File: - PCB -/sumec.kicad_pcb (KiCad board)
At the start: 2 copper layers, 95 x 73 mm, 30 parts, among them IC1 XT30U-F, SW1 SW_SPDT, SW3 SW_Push, U1 ESP32-DEVKIT-V1, U10 LD1117AV33, U11 ROB-14450, U2 VL53L0X, U3 VL53L0X, U4 VL53L0X, U5 TSOP382xx, U6 QRE1113, U7 QRE1113, U8 QRE1113, U9 QRE1113

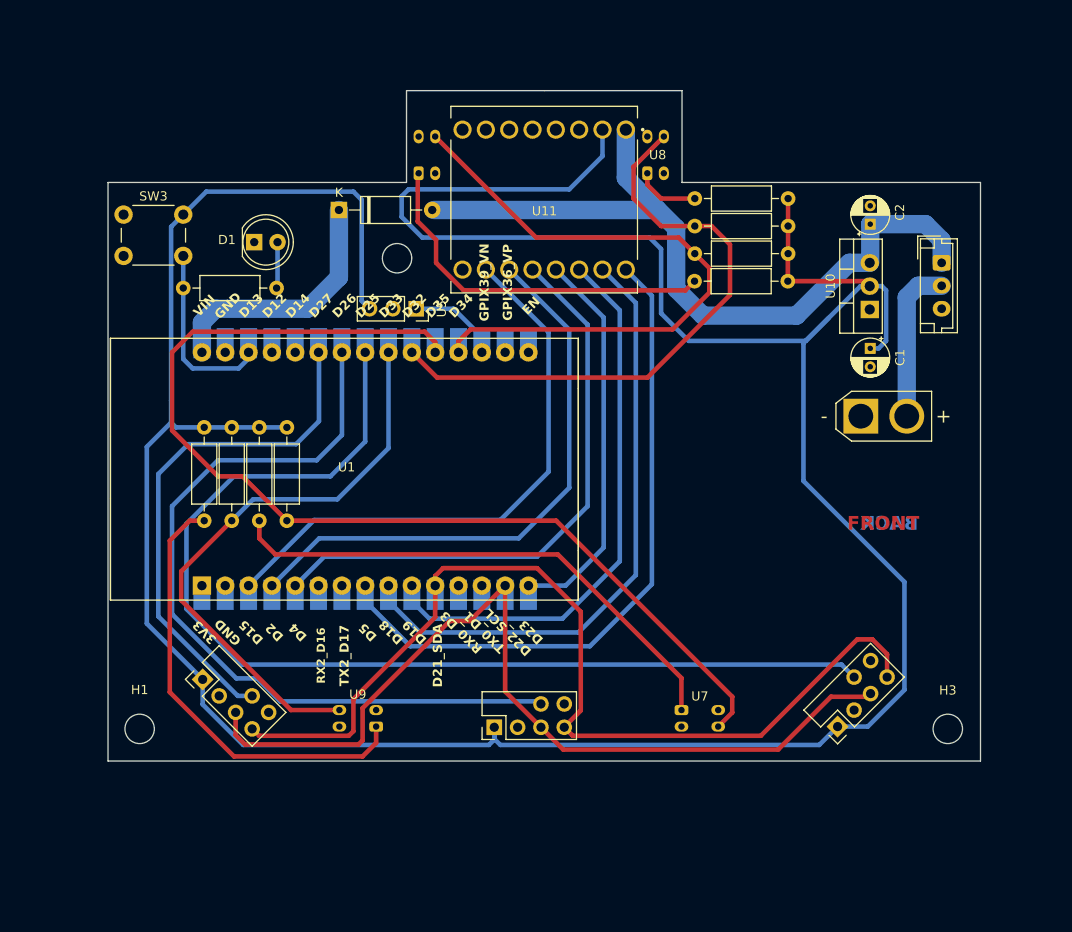
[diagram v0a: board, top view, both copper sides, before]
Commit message: PCB almost wired
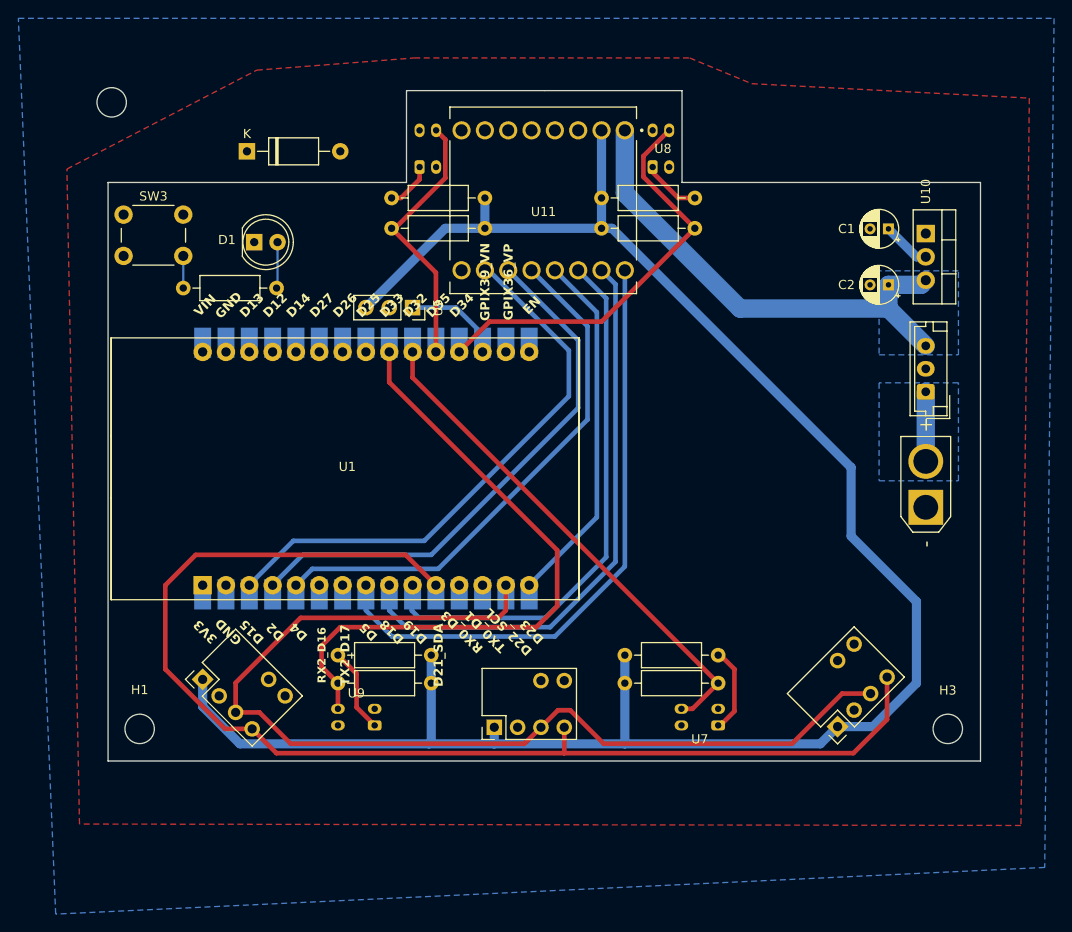
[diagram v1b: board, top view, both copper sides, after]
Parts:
- moved R4 52.1 mm to (156.5, 109.5), turned to 180 degrees
- moved R5 46.2 mm to (146.3, 112.5), turned to 0 degrees
- moved H2 35.4 mm to (90.4, 49.3)
- moved R9 35.3 mm to (125.2, 112.5), turned to 180 degrees
- moved R2 34.2 mm to (120.9, 59.7)
- moved R3 33.1 mm to (131.1, 63.0)
- moved R8 20.7 mm to (115.1, 109.5), turned to 0 degrees
- moved R7 20.3 mm to (143.8, 63.0), turned to 0 degrees
- moved SW1 14.1 mm to (179.1, 80.8), turned to 90 degrees
- moved C1 13.2 mm to (175.0, 63.1), turned to 180 degrees
- moved IC1 12.2 mm to (179.1, 93.4), turned to 90 degrees
- moved D2 11.9 mm to (105.2, 54.6)
- moved U10 10.3 mm to (179.1, 63.6), turned to -90 degrees
- moved C2 6.90 mm to (175.0, 69.1), turned to 180 degrees
- moved U7 4.33 mm to (156.5, 117.1), turned to 90 degrees
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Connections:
- SW1 pad 1: +12V -> 12V IN
- SW1 pad 2: 12V IN -> unconnected-(SW1A-B-Pad2)
- SW1 pad 3: unconnected-(SW1A-C-Pad3) -> +12V
- U1 pad 19: QRE1113 A -> QRE1113 C
- U1 pad 20: QRE1113 B -> QRE1113 A
- U1 pad 21: QRE1113 C -> QRE1113 B
- U1 pad 23: X-SHUT 2 -> X-SHUT 1
- U1 pad 24: X-SHUT 3 -> X-SHUT 2
- U1 pad 25: X-SHUT 1 -> X-SHUT 3
- U2 pad 5: GPIO -> unconnected-(U2-GPIO-Pad5)
- U3 pad 5: GPIO -> unconnected-(U3-GPIO-Pad5)
- U4 pad 5: GPIO -> unconnected-(U4-GPIO-Pad5)
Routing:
- net +3V3: track 353.5 -> 219.2 mm
- net X-SHUT 2: track 117.9 -> 0.00 mm
- net X-SHUT 3: track 86.7 -> 0.00 mm
- net QRE1113 B: track 116.6 -> 55.0 mm
- net X-SHUT 1: track 56.7 -> 0.00 mm
- net Net-(U7-A): track 57.7 -> 9.40 mm
- net QRE1113 A: track 69.2 -> 29.2 mm
- net Net-(U9-A): track 48.9 -> 9.30 mm
- net Net-(U6-A): track 40.4 -> 5.22 mm
- net +12V: track 84.0 -> 53.4 mm
- net Net-(D2-K): track 27.5 -> 0.00 mm
- net SDA: track 106.7 -> 132.7 mm
- net QRE1113 C: track 65.7 -> 45.4 mm
- net SCL: track 97.9 -> 114.5 mm
- net TEST PROGRAM: track 19.9 -> 3.50 mm
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- added copper zone on B.Cu, net +12V
- added copper zone on B.Cu, net 12V IN
- added copper zone on B.Cu, net GND
- added copper zone on F.Cu, net GND
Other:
- board text removed: "BACK"
- board text removed: "FRONT"

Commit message: PCB - Board update
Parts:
- moved H2 74.0 mm to (163.2, 62.2)
- moved D2 31.4 mm to (136.1, 60.0)
- moved R3 19.8 mm to (113.2, 71.7), turned to 45 degrees
- moved R4 10.4 mm to (146.2, 107.5), turned to -90 degrees
- moved R5 6.00 mm to (149.5, 117.6), turned to 90 degrees
- moved R9 5.99 mm to (129.2, 117.0), turned to 135 degrees
- moved R8 3.97 mm to (118.8, 110.8), turned to -45 degrees
- moved R2 3.59 mm to (118.4, 62.3), turned to -135 degrees
- moved U11 1.41 mm to (137.4, 61.4)
- moved SW3 1.22 mm to (91.7, 62.7)
- moved R1 0.72 mm to (98.2, 70.2)
- moved D1 0.22 mm to (106.0, 64.7)
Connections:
- U1 pad 23: X-SHUT 1 -> X-SHUT 2
- U1 pad 24: X-SHUT 2 -> X-SHUT 3
- U1 pad 25: X-SHUT 3 -> X-SHUT 1
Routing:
- net X-SHUT 2: track 0.00 -> 110.4 mm
- net X-SHUT 3: track 0.00 -> 80.8 mm
- net Net-(D2-K): track 0.00 -> 58.9 mm
- net +3V3: track 219.2 -> 275.8 mm
- net X-SHUT 1: track 0.00 -> 53.4 mm
- net Net-(U7-A): track 9.40 -> 22.8 mm
- net TEST PROGRAM: track 3.50 -> 14.6 mm
- net QRE1113 D: track 70.3 -> 73.7 mm
- net Net-(U6-A): track 5.22 -> 8.40 mm
- net QRE1113 B: track 55.0 -> 57.8 mm
- net BI1: track 58.0 -> 55.6 mm
- net PWMB: track 61.1 -> 58.7 mm
- net BI2: track 59.4 -> 57.2 mm
- net STBY: track 39.2 -> 37.2 mm
- net AI1: track 59.4 -> 57.6 mm
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
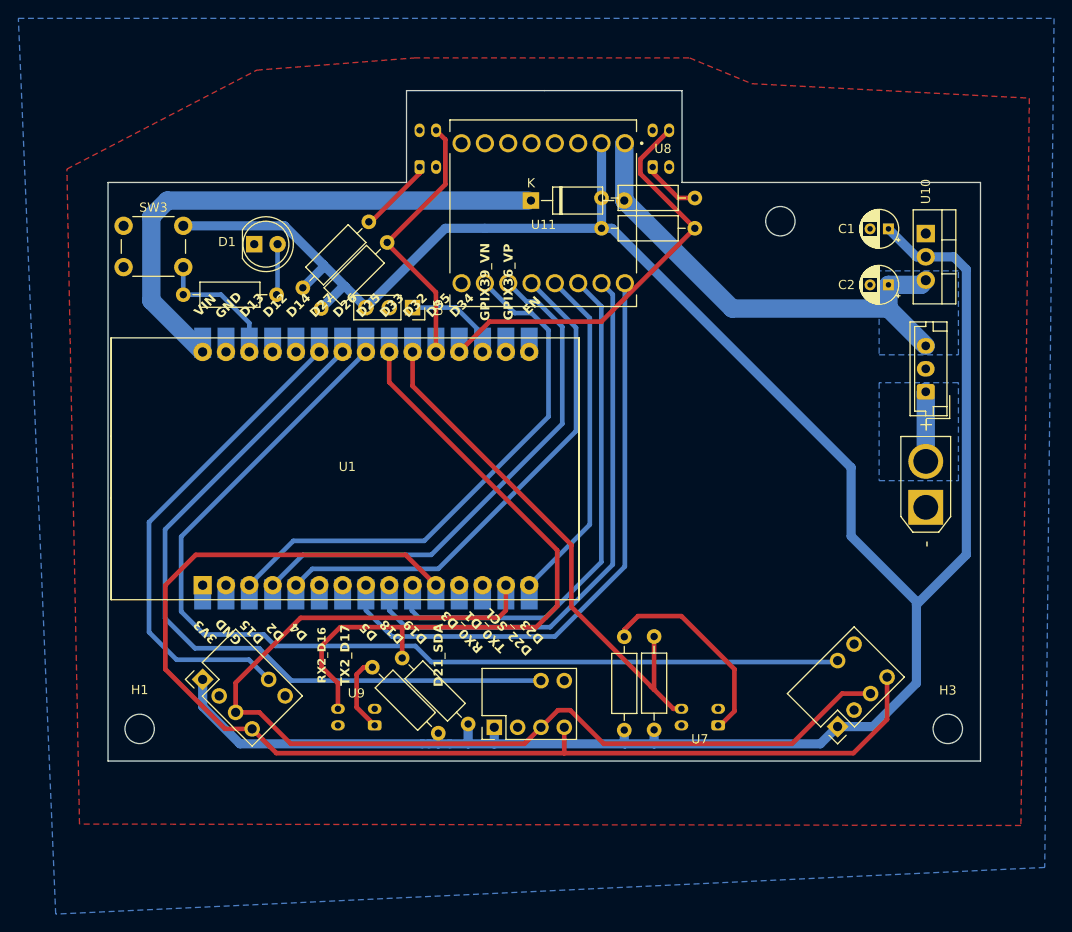
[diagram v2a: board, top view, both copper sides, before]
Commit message: PCB - Wiring control and fix
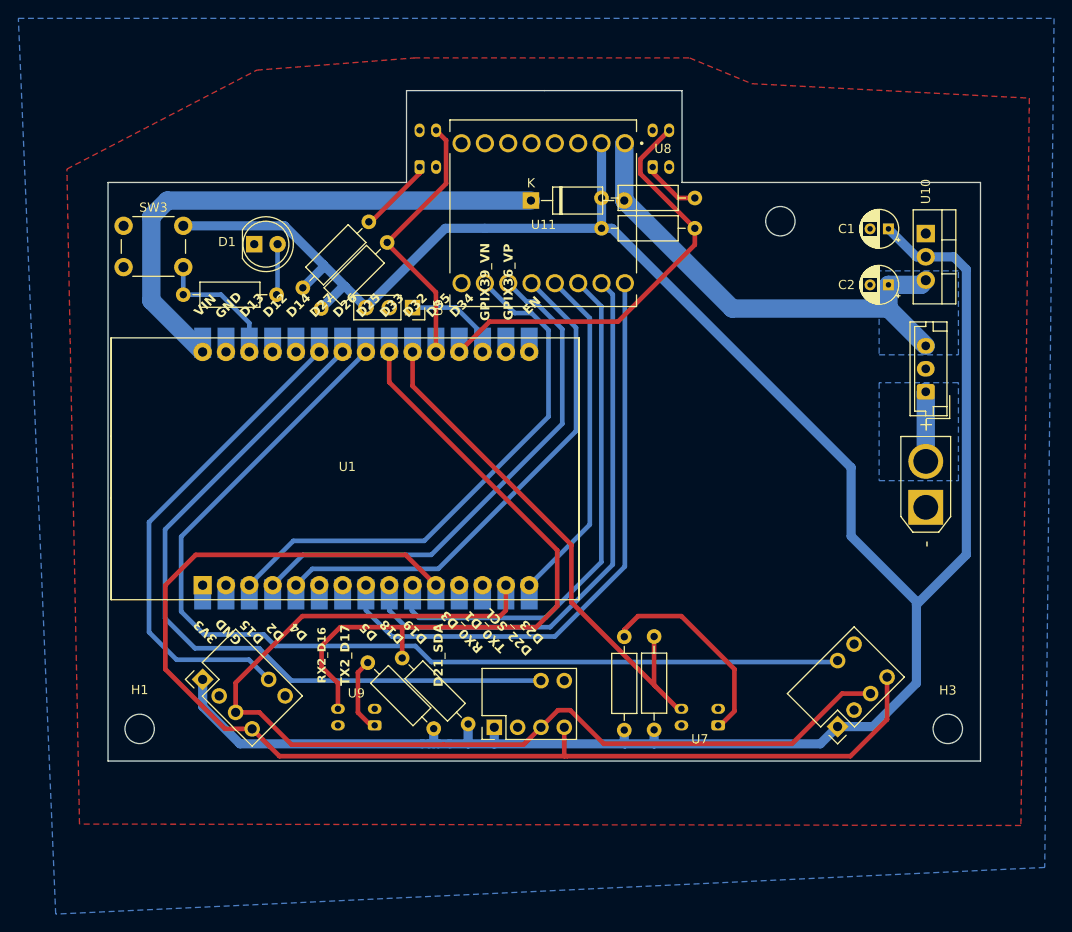
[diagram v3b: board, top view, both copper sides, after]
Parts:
- moved R8 0.71 mm to (118.3, 110.3)
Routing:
- net QRE1113 B: track 57.8 -> 56.7 mm
- net QRE1113 C: track 45.7 -> 46.7 mm
- net SDA: track 132.7 -> 133.3 mm

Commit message: PCB - LED Signal. board upd
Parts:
- R1: value 75 -> 75
- moved R1 7.00 mm to (102.3, 64.5), turned to -45 degrees
- moved D1 6.92 mm to (103.0, 71.0), turned to 135 degrees
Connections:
- R1 pad 1: TEST PROGRAM -> Net-(D1-A)
- R1 pad 2: Net-(D1-A) -> LED SIGNALISATION
- U1 pad 26: unconnected-(U1-D14-Pad26) -> LED SIGNALISATION
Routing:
- net LED SIGNALISATION: track 0.00 -> 5.15 mm
- net Net-(D1-A): track 4.83 -> 5.72 mm

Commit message: Update sumec.kicad_pcb
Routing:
- net QRE1113 D: track 73.7 -> 70.7 mm
- net QRE1113 B: track 56.7 -> 58.9 mm
- net QRE1113 C: track 46.7 -> 48.3 mm
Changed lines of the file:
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@@
   (segment (start 123.19 80.17) (end 140.49 97.47) (width 0.508) (layer "F.Cu") (net 9))
   (segment (start 152.086 115.316) (end 152.464 115.316) (width 0.508) (layer "F.Cu") (net 9))
-  (segment (start 149.615 112.845) (end 149.49 112.72) (width 0.508) (layer "F.Cu") (net 9))
   (segment (start 140.49 97.47) (end 140.49 103.72) (width 0.508) (layer "F.Cu") (net 9))
   (segment (start 123.19 76.454) (end 123.19 80.17) (width 0.508) (layer "F.Cu") (net 9))
   (segment (start 149.615 112.845) (end 152.086 115.316) (width 0.508) (layer "F.Cu") (net 9))
-  (segment (start 149.49 112.72) (end 149.49 107.442) (width 0.508) (layer "F.Cu") (net 9))
+  (segment (start 149.615 112.845) (end 146.851 110.081) (width 0.508) (layer "F.Cu") (net 9))
   (segment (start 140.49 103.72) (end 149.615 112.845) (width 0.508) (layer "F.Cu") (net 9))
+  (segment (start 146.851 110.081) (end 149.49 107.442) (width 0.508) (layer "F.Cu") (net 9))
   (segment (start 152.124 59.69) (end 153.924 59.69) (width 0.508) (layer "F.Cu") (net 10))
   (segment (start 149.33 56.896) (end 152.124 59.69) (width 0.508) (layer "F.Cu") (net 10))
+  (segment (start 151.13 52.324) (end 147.99 55.464) (width 0.508) (layer "F.Cu") (net 11))
+  (segment (start 128.8288 73.152) (end 145.558 73.152) (width 0.508) (layer "F.Cu") (net 11))
+  (segment (start 147.99 57.058) (end 153.924 62.992) (width 0.508) (layer "F.Cu") (net 11))
+  (segment (start 153.924 64.786) (end 153.924 62.992) (width 0.508) (layer "F.Cu") (net 11))
+  (segment (start 128.27 76.454) (end 128.27 73.7108) (width 0.508) (layer "F.Cu") (net 11))
+  (segment (start 128.27 73.7108) (end 128.8288 73.152) (width 0.508) (layer "F.Cu") (net 11))
   (segment (start 145.558 73.152) (end 153.924 64.786) (width 0.508) (layer "F.Cu") (net 11))
-  (segment (start 151.13 52.324) (end 147.99 55.464) (width 0.508) (layer "F.Cu") (net 11))
-  (segment (start 147.99 57.058) (end 153.924 62.992) (width 0.508) (layer "F.Cu") (net 11))
-  (segment (start 128.27 76.454) (end 131.572 73.152) (width 0.508) (layer "F.Cu") (net 11))
-  (segment (start 153.924 64.786) (end 153.924 62.992) (width 0.508) (layer "F.Cu") (net 11))
   (segment (start 147.99 55.464) (end 147.99 57.058) (width 0.508) (layer "F.Cu") (net 11))
-  (segment (start 131.572 73.152) (end 145.558 73.152) (width 0.508) (layer "F.Cu") (net 11))
   (segment (start 118.636 117.116) (end 119.062 117.116) (width 0.508) (layer "F.Cu") (net 12))
   (segment (start 117.24 111.35159) (end 117.24 115.72) (width 0.508) (layer "F.Cu") (net 12))
   (segment (start 118.305795 110.285795) (end 117.24 111.35159) (width 0.508) (layer "F.Cu") (net 12))
   (segment (start 117.24 115.72) (end 118.636 117.116) (width 0.508) (layer "F.Cu") (net 12))
+  (segment (start 118.0592 106.426) (end 115.062 109.4232) (width 0.508) (layer "F.Cu") (net 13))
   (segment (start 120.65 76.454) (end 120.65 79.756) (width 0.508) (layer "F.Cu") (net 13))
   (segment (start 136.652 106.426) (end 122.24 106.426) (width 0.508) (layer "F.Cu") (net 13))
-  (segment (start 113.284 110.744) (end 115.062 112.522) (width 0.508) (layer "F.Cu") (net 13))
   (segment (start 122.055795 106.610205) (end 122.055795 109.785795) (width 0.508) (layer "F.Cu") (net 13))
   (segment (start 138.938 98.044) (end 138.938 104.14) (width 0.508) (layer "F.Cu") (net 13))
   (segment (start 122.24 106.426) (end 122.055795 106.610205) (width 0.508) (layer "F.Cu") (net 13))
-  (segment (start 113.284 108.458) (end 113.284 110.744) (width 0.508) (layer "F.Cu") (net 13))
-  (segment (start 122.24 106.426) (end 115.316 106.426) (width 0.508) (layer "F.Cu") (net 13))
-  (segment (start 115.316 106.426) (end 113.284 108.458) (width 0.508) (layer "F.Cu") (net 13))
-  (segment (start 115.062 112.522) (end 115.062 115.316) (width 0.508) (layer "F.Cu") (net 13))
+  (segment (start 122.24 106.426) (end 118.0592 106.426) (width 0.508) (layer "F.Cu") (net 13))
+  (segment (start 115.062 109.4232) (end 115.062 115.316) (width 0.508) (layer "F.Cu") (net 13))
   (segment (start 120.65 79.756) (end 138.938 98.044) (width 0.508) (layer "F.Cu") (net 13))
   (segment (start 138.938 104.14) (end 136.652 106.426) (width 0.508) (layer "F.Cu") (net 13))
@@
   (segment (start 142.49 95.254) (end 135.89 101.854) (width 0.508) (layer "B.Cu") (net 24))
   (segment (start 138.684 68.97) (end 142.49 72.776) (width 0.508) (layer "B.Cu") (net 24))
+  (segment (start 140.99 85.07) (end 125.984 100.076) (width 0.508) (layer "B.Cu") (net 25))
   (segment (start 140.99 73.816) (end 140.99 85.07) (width 0.508) (layer "B.Cu") (net 25))
-  (segment (start 140.99 85.07) (end 125.984 100.076) (width 0.508) (layer "B.Cu") (net 25))
   (segment (start 125.984 100.076) (end 112.268 100.076) (width 0.508) (layer "B.Cu") (net 25))
   (segment (start 136.144 68.97) (end 140.99 73.816) (width 0.508) (layer "B.Cu") (net 25))
@@
   (segment (start 131.064 68.97) (end 134.314 72.22) (width 0.508) (layer "B.Cu") (net 27))
   (segment (start 136.134 72.22) (end 137.99 74.076) (width 0.508) (layer "B.Cu") (net 27))
-  (segment (start 147.74 105.22) (end 152.464 105.22) (width 0.508) (layer "F.Cu") (net 28))
-  (segment (start 146.24 106.72) (end 147.74 105.22) (width 0.508) (layer "F.Cu") (net 28))
+  (segment (start 146.24 107.47) (end 148.49 105.22) (width 0.508) (layer "F.Cu") (net 28))
+  (segment (start 148.49 105.22) (end 152.464 105.22) (width 0.508) (layer "F.Cu") (net 28))
+  (segment (start 152.464 105.22) (end 158.242 110.998) (width 0.508) (layer "F.Cu") (net 28))
+  (segment (start 158.242 110.998) (end 158.242 115.57) (width 0.508) (layer "F.Cu") (net 28))
+  (segment (start 156.696 117.116) (end 156.464 117.116) (width 0.508) (layer "F.Cu") (net 28))
   (segment (start 158.242 115.57) (end 156.696 117.116) (width 0.508) (layer "F.Cu") (net 28))
-  (segment (start 146.24 107.47) (end 146.24 106.72) (width 0.508) (layer "F.Cu") (net 28))
-  (segment (start 156.696 117.116) (end 156.464 117.116) (width 0.508) (layer "F.Cu") (net 28))
-  (segment (start 158.242 110.998) (end 158.242 115.57) (width 0.508) (layer "F.Cu") (net 28))
-  (segment (start 152.464 105.22) (end 158.242 110.998) (width 0.508) (layer "F.Cu") (net 28))
   (segment (start 94.49 106.97) (end 94.49 94.994) (width 0.508) (layer "B.Cu") (net 32))
   (segment (start 105.374204 109.97) (end 97.49 109.97) (width 0.508) (layer "B.Cu") (net 32))
@@
   (segment (start 107.516051 112.111847) (end 105.374204 109.97) (width 0.508) (layer "B.Cu") (net 32))
   (segment (start 169.47 110.065795) (end 169.315795 110.22) (width 0.25) (layer "B.Cu") (net 33))
-  (segment (start 97.99 96.574) (end 97.99 104.72) (width 0.508) (layer "B.Cu") (net 33))
-  (segment (start 97.99 104.72) (end 100.49 107.22) (width 0.508) (layer "B.Cu") (net 33))
   (segment (start 100.49 107.22) (end 106.99 107.22) (width 0.508) (layer "B.Cu") (net 33))
   (segment (start 106.99 107.22) (end 108.24 108.47) (width 0.508) (layer "B.Cu") (net 33))
-  (segment (start 108.24 108.47) (end 123.49 108.47) (width 0.508) (layer "B.Cu") (net 33))
+  (segment (start 97.99 104.72) (end 100.49 107.22) (width 0.508) (layer "B.Cu") (net 33))
+  (segment (start 124.594595 110.065795) (end 169.47 110.065795) (width 0.508) (layer "B.Cu") (net 33))
+  (segment (start 122.9988 108.47) (end 124.594595 110.065795) (width 0.508) (layer "B.Cu") (net 33))
+  (segment (start 108.24 108.47) (end 122.9988 108.47) (width 0.508) (layer "B.Cu") (net 33))
+  (segment (start 97.99 96.574) (end 97.99 104.72) (width 0.508) (layer "B.Cu") (net 33))
   (segment (start 118.11 76.454) (end 97.99 96.574) (width 0.508) (layer "B.Cu") (net 33))
-  (segment (start 125.24 110.22) (end 169.315795 110.22) (width 0.508) (layer "B.Cu") (net 33))
-  (segment (start 123.49 108.47) (end 125.24 110.22) (width 0.508) (layer "B.Cu") (net 33))
   (segment (start 106.49 108.72) (end 99.49 108.72) (width 0.508) (layer "B.Cu") (net 34))
   (segment (start 96.24 95.784) (end 115.57 76.454) (width 0.508) (layer "B.Cu") (net 34))
@@
     (connect_pads yes (clearance 0.5))
     (min_thickness 0.25) (filled_areas_thickness no)
-    (fill yes (thermal_gap 0.5) (thermal_bridge_width 0.5))
+    (fill yes (thermal_gap 0.5) (thermal_bridge_width 0.5) (smoothing fillet) (radius 1))
     (polygon
       (pts
